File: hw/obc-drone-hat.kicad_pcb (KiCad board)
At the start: 4 copper layers, 65 x 56.5 mm, 68 parts, among them SW1 SW_DIP_x04

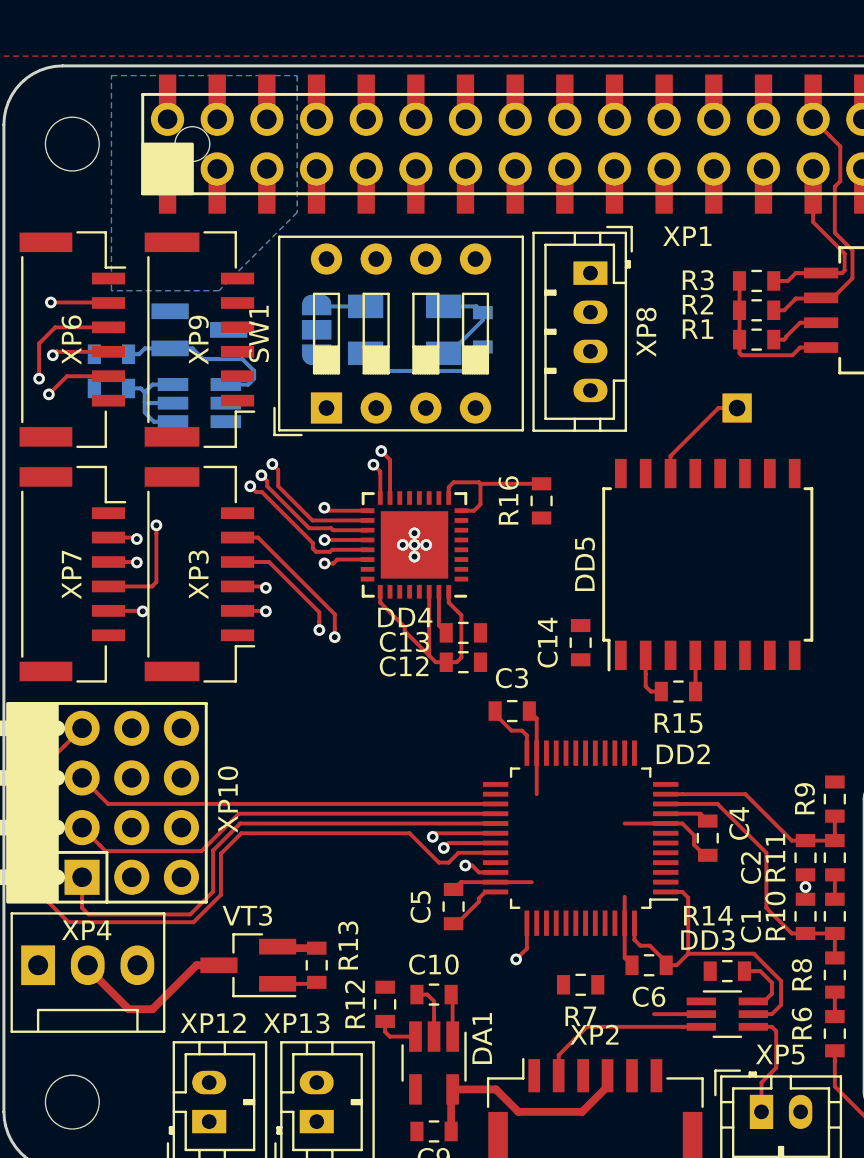
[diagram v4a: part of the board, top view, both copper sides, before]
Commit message: hw: partial route SPI
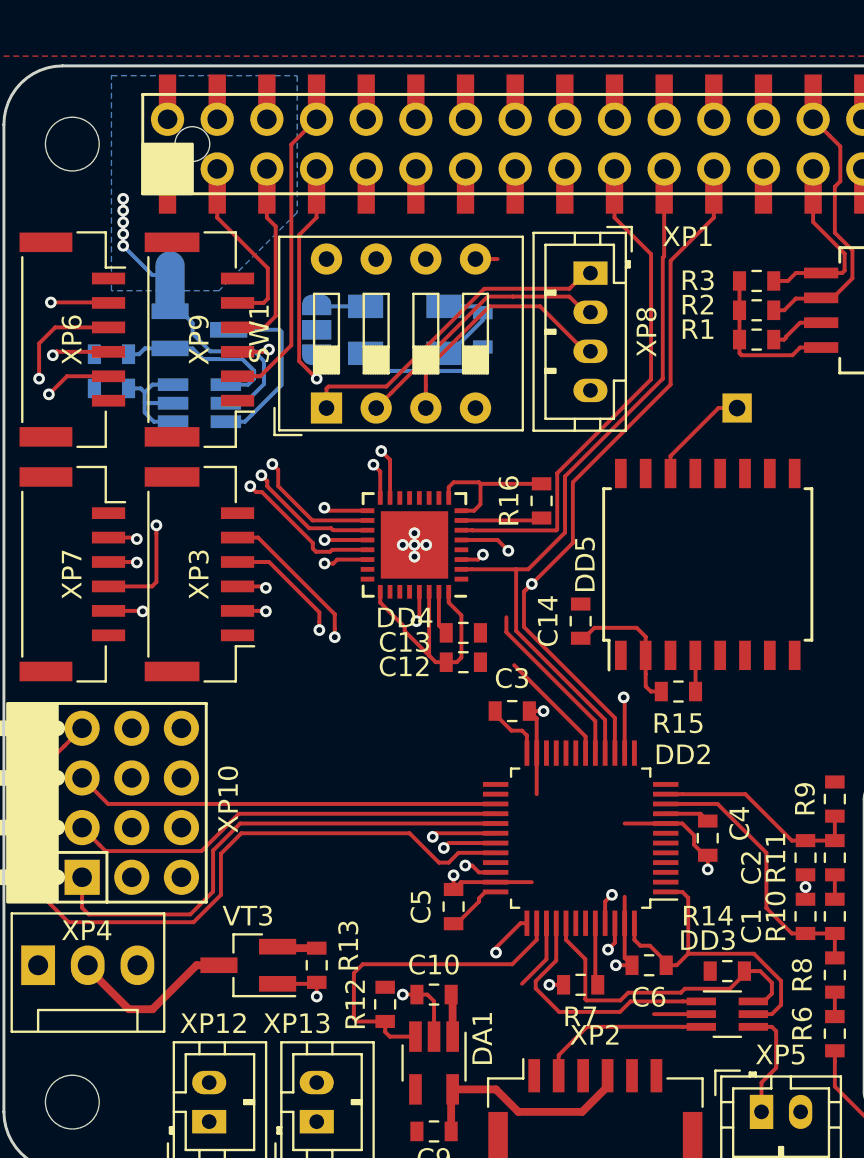
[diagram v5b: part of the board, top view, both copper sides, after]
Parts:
- moved C14 1.10 mm to (159.5, 111.9)
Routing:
- net RPI_SPI0_SCLK: track 1.45 -> 40.7 mm, vias 0 -> 2
- net RPI_SPI0_MISO: track 1.45 -> 40.4 mm
- net ~RPI_SPI0_CE1: track 1.45 -> 36.9 mm, vias 0 -> 1
- net RPI_SPI0_MOSI: track 1.45 -> 35.0 mm
- net ~RPI_SPI0_CE0: track 1.45 -> 30.5 mm, vias 0 -> 1
- net /RC IO MCU/FAN_RPM: track 0.00 -> 27.7 mm, vias 0 -> 1
- net /RC IO MCU/~FAN_PWM: track 2.03 -> 21.6 mm, vias 0 -> 2
- net +5VP: track 5.08 -> 22.5 mm, vias 0 -> 5
- net CFG_ID0: track 1.45 -> 18.4 mm
- net RPI_RX: track 1.45 -> 18.2 mm, vias 0 -> 1
- net RPI_TX: track 1.45 -> 16.9 mm
- net /RC IO MCU/~Rx_EN: track 2.18 -> 17.1 mm
- net CFG_ID1: track 1.45 -> 15.1 mm
- net /RC IO MCU/CPPM_SEL: track 3.32 -> 16.5 mm
- net /RC IO MCU/STM_CPPM: track 0.00 -> 13.0 mm
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
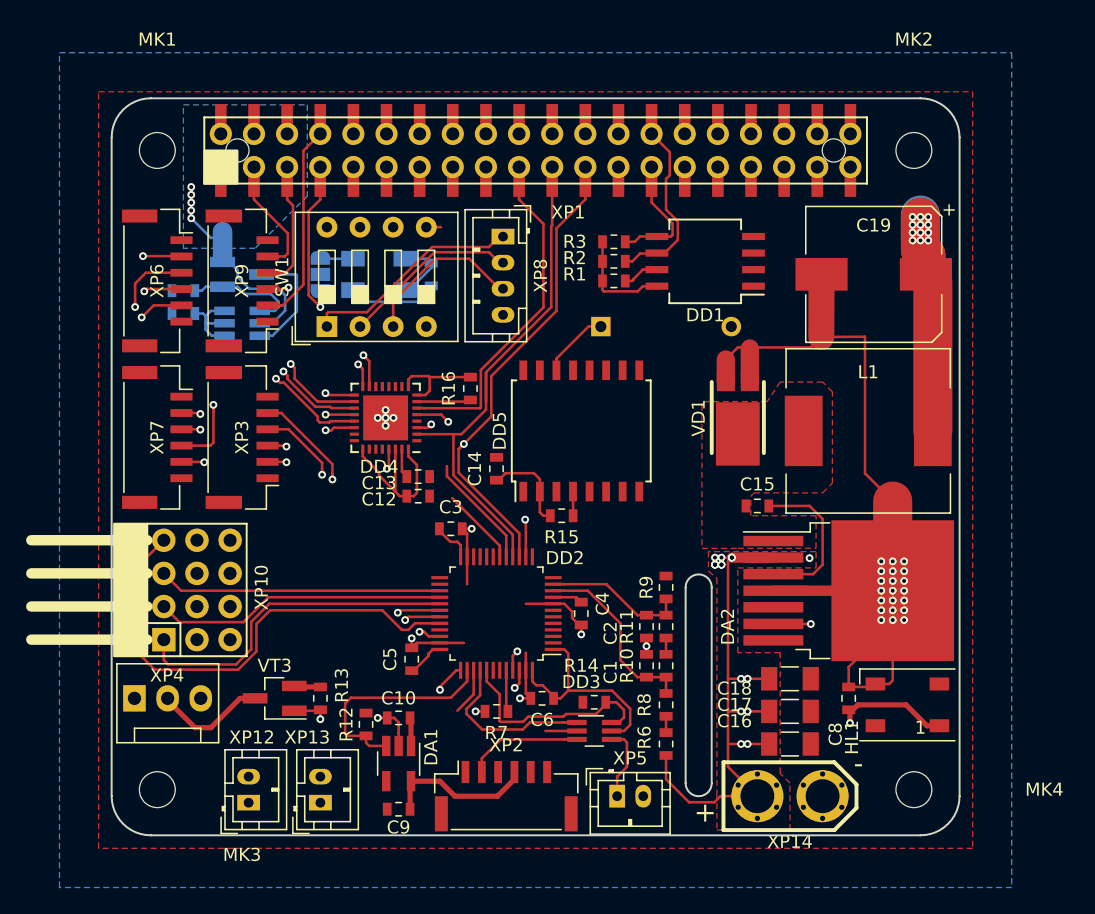
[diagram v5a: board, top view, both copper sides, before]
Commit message: hw: 11 unc left
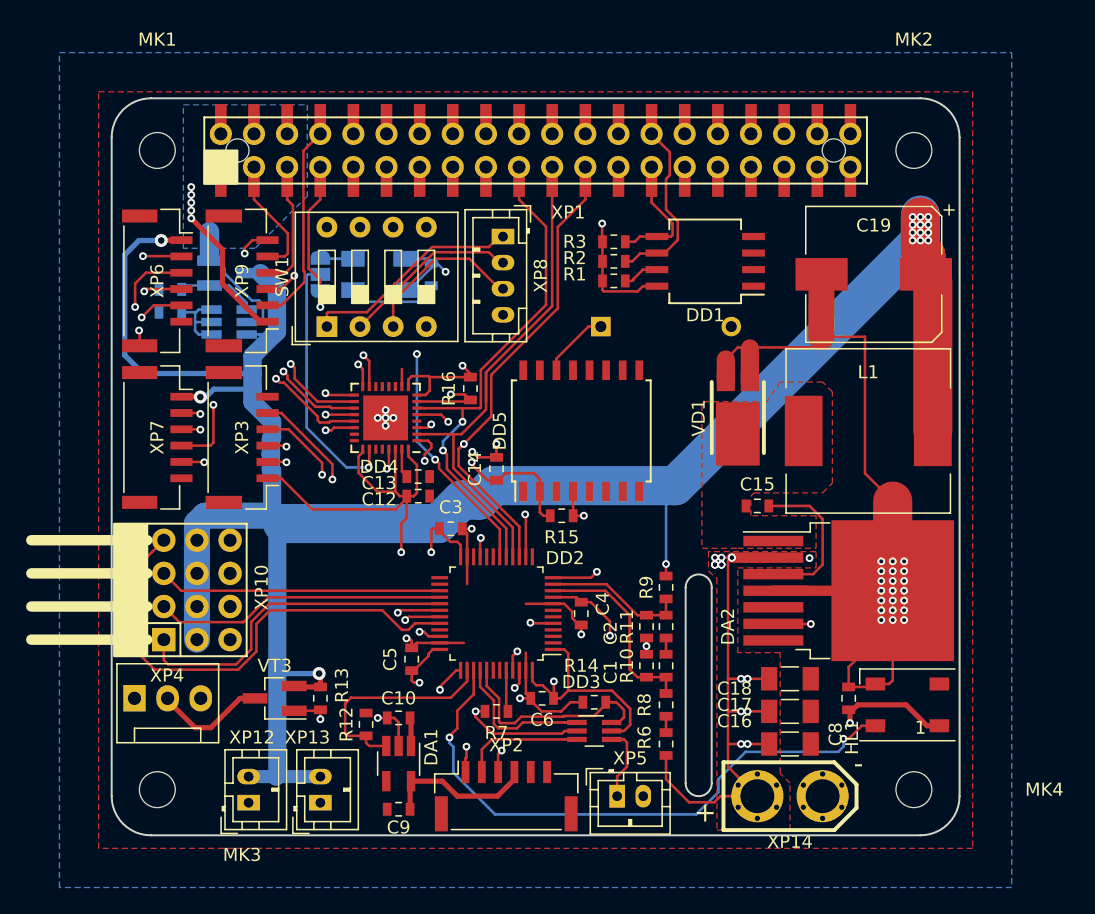
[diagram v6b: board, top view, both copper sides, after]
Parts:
- moved R4 1.00 mm to (134.5, 99.9)
- moved R5 1.00 mm to (134.5, 98.2)
- moved VT1 1.00 mm to (139.0, 96.9)
- moved VT2 1.00 mm to (139.0, 100.7)
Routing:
- net +5Vhat: track 142.6 -> 296.1 mm, vias 14 -> 18
- net +3.3VP: track 69.2 -> 209.5 mm, vias 0 -> 9
- net /RC IO MCU/WS_DOUT: track 3.61 -> 46.2 mm, vias 0 -> 2
- net HAT_CLK: track 0.00 -> 39.3 mm, vias 0 -> 2
- net /RC IO MCU/Rx_S.port: track 0.00 -> 32.5 mm, vias 0 -> 2
- net ~STM_INT: track 7.46 -> 38.4 mm, vias 0 -> 2
- net /RC IO MCU/Rx_SBUS: track 0.00 -> 25.3 mm, vias 0 -> 2
- net ~SER_IRQ: track 5.60 -> 29.4 mm, vias 0 -> 1
- net ~HAT_RST: track 1.85 -> 20.6 mm, vias 0 -> 2
- net GND: track 140.9 -> 159.3 mm, vias 34 -> 38
- net +5VP: track 22.5 -> 30.0 mm
- net RPI_SPI0_MOSI: track 35.0 -> 40.3 mm, vias 0 -> 2
- net /RPi/ZVD_G: track 9.00 -> 6.72 mm
- net ~RPI_SPI0_CE0: track 30.5 -> 32.6 mm
- net /RC IO MCU/STM_CPPM: track 13.0 -> 11.2 mm
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
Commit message: hw: routing done
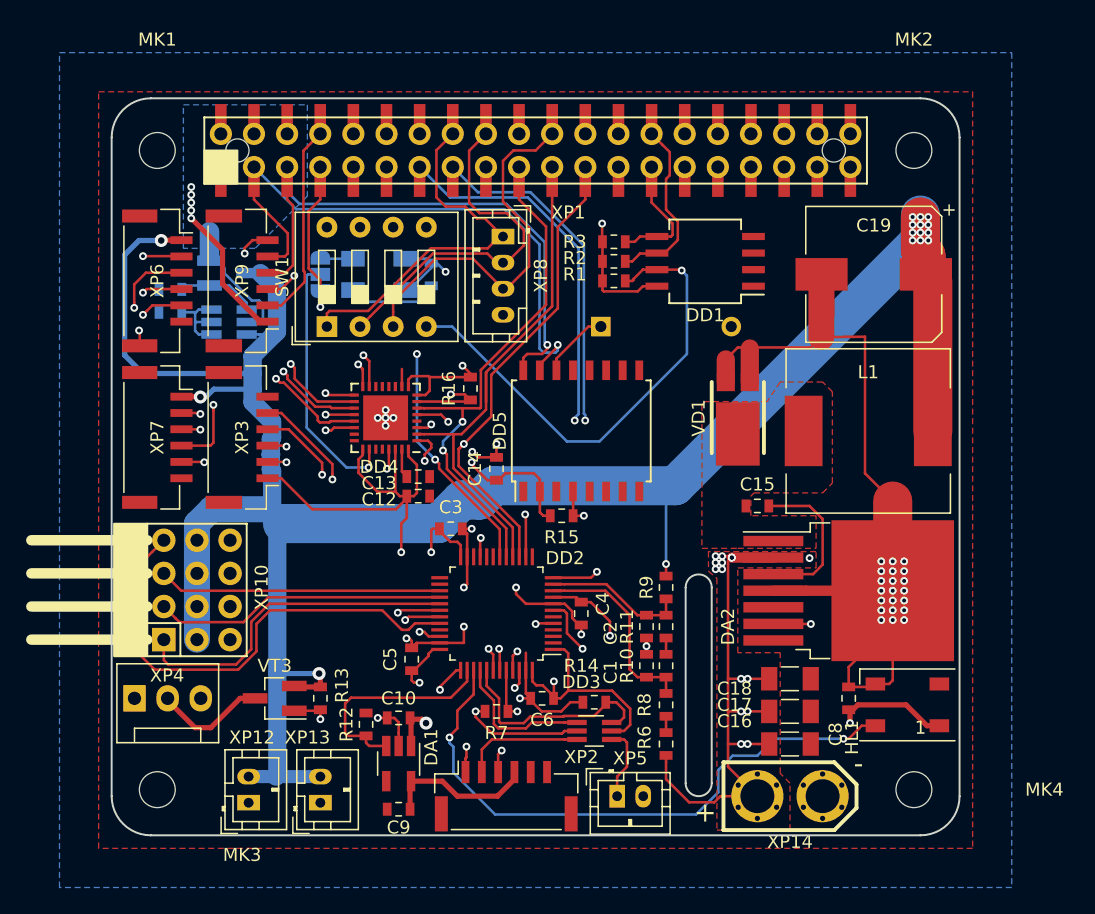
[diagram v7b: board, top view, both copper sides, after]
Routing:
- net RPI_SDA: track 9.35 -> 73.1 mm, vias 0 -> 2
- net RPI_SCL: track 9.90 -> 71.5 mm, vias 0 -> 2
- net STM_BOOT0: track 4.65 -> 61.5 mm, vias 0 -> 2
- net ~STM_RESET: track 1.45 -> 54.3 mm, vias 0 -> 2
- net +5VP: track 30.0 -> 77.5 mm, vias 5 -> 6
- net ~HAT_ID_WE: track 2.81 -> 37.7 mm, vias 0 -> 1
- net CFG_ID2: track 14.1 -> 30.4 mm
- net CFG_ID1: track 15.1 -> 29.2 mm
- net CFG_ID0: track 18.4 -> 30.1 mm
- net GND: track 159.3 -> 162.5 mm, vias 38 -> 41
- net /UART/~U1_RTS: track 14.4 -> 16.2 mm
- net Vbat: track 44.1 -> 45.0 mm

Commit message: hw: small route optimizations
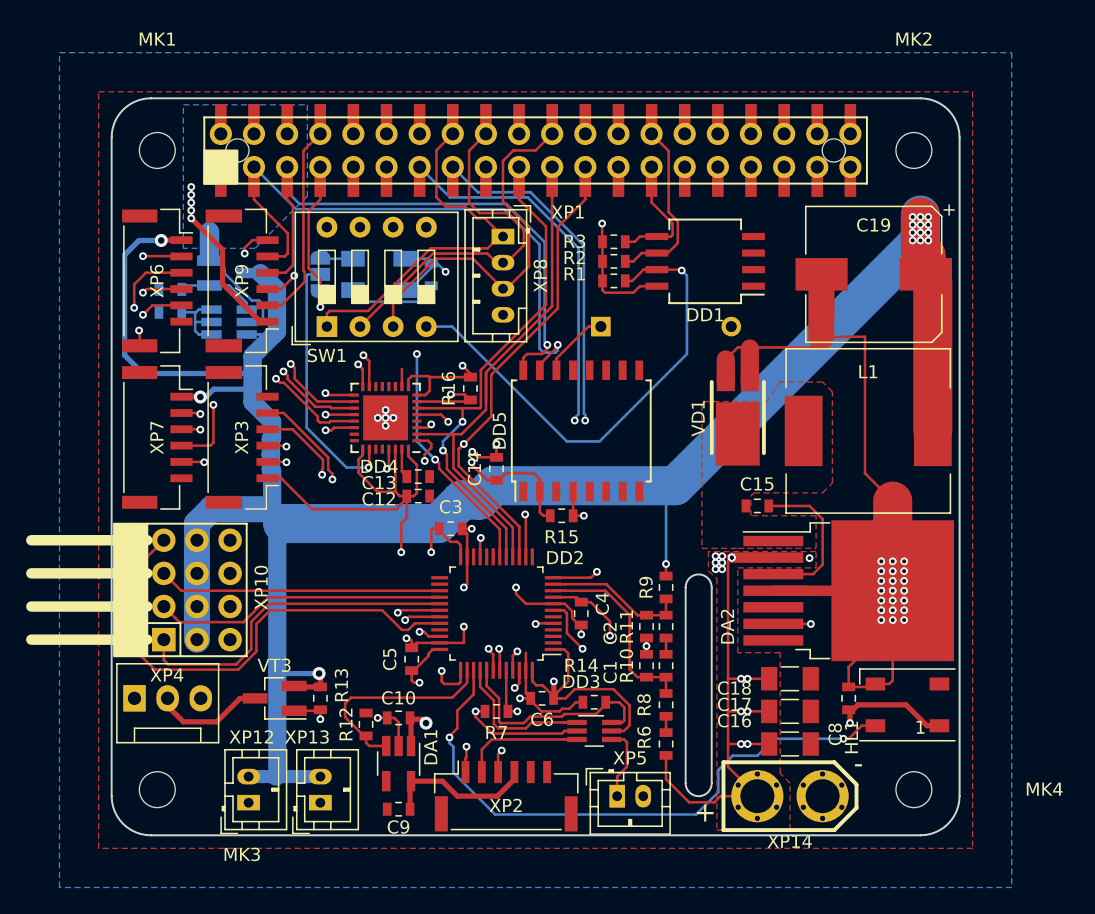
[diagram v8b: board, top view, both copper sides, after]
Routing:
- net GND: track 162.5 -> 167.9 mm
- net RPI_RX: track 18.0 -> 16.7 mm
- net ~SER_IRQ: track 29.4 -> 28.2 mm
- net +3.3VP: track 209.6 -> 210.8 mm
- net ~STM_INT: track 38.4 -> 37.5 mm
- net /RC IO MCU/SWCLK: track 30.2 -> 29.3 mm
- net /RC IO MCU/~Rx_EN: track 17.1 -> 16.4 mm
